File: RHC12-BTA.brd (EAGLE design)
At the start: 20 x 40 mm, 6 parts

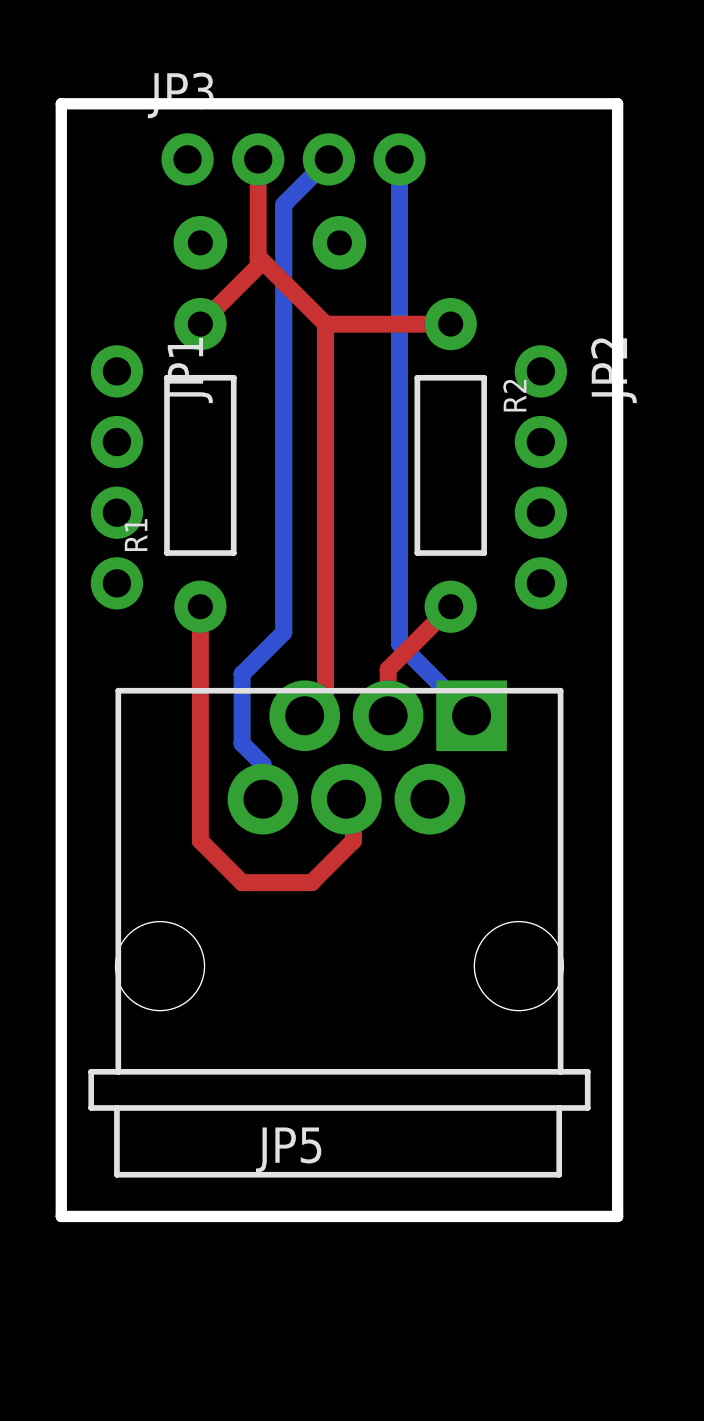
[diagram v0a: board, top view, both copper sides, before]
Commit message: Switched RHC12 to SMD except for the BTA part
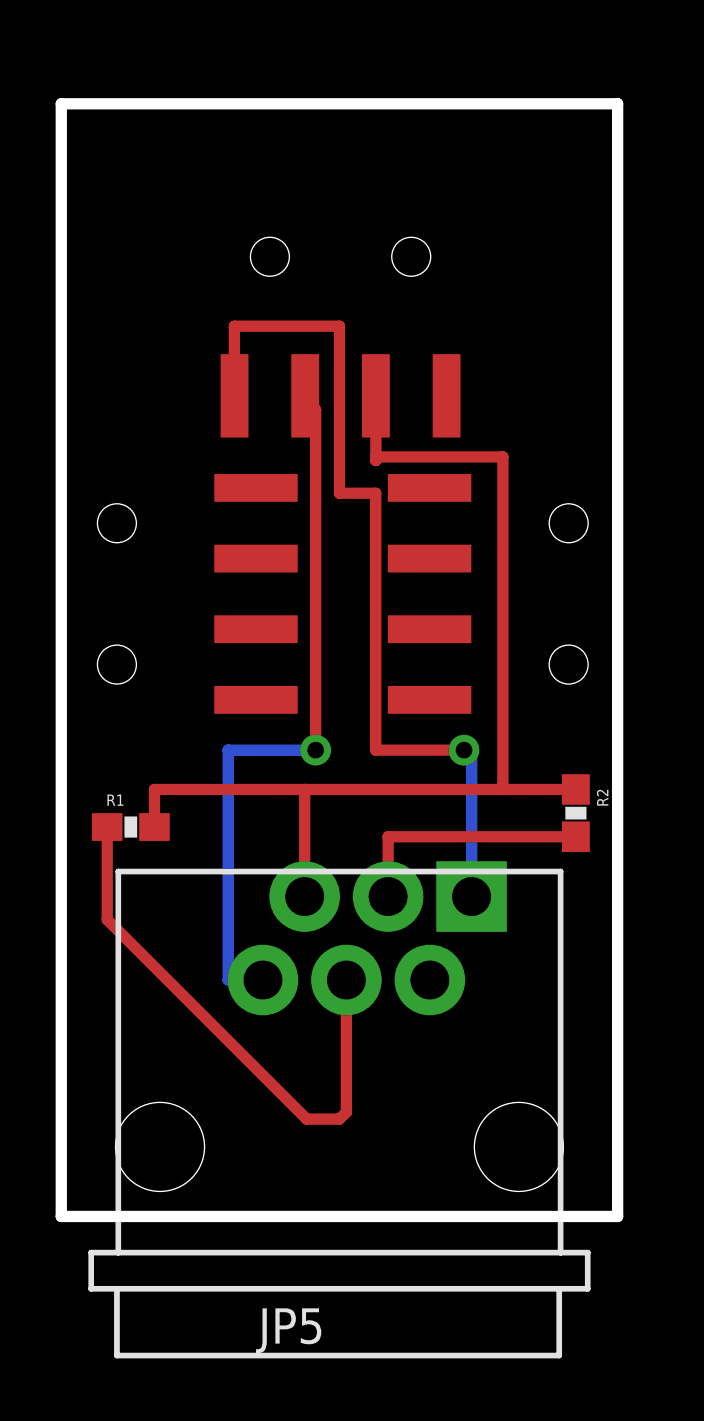
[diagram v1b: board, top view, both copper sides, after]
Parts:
- JP1, JP2, JP3: device SparkFun-Connectors:1X04_NO_SILK_ALL_ROUND -> SparkFun-Connectors:1X04-SMD
- R1, R2: device SparkFun-Passives:AXIAL-0.4 -> SparkFun-Passives:0603-RES
- moved R2 13.3 mm to (18.5, 14.5)
- moved R1 13.2 mm to (2.50, 14.0), turned to 0 degrees
- moved JP2 8.06 mm to (18.2, 22.4), turned to 90 degrees
- moved JP1 8.00 mm to (2.00, 22.4)
- moved JP3 6.52 mm to (10.0, 34.5), turned to 180 degrees
- moved JP5 6.50 mm to (10.0, 2.50)
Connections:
- net 5V: now also R1.2, R2.1; no longer R1.P$2, R2.P$1
- net N$1: now also R1.1; no longer R1.P$1
- net N$3: now also R2.2; no longer R2.P$2
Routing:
- net S2: track 21.1 -> 31.5 mm, vias 0 -> 1
- net 5V: track 29.1 -> 39.3 mm
- net N$3: track 4.85 -> 8.90 mm
- net N$1: track 16.8 -> 19.8 mm
- net S1: track 24.6 -> 27.6 mm, vias 0 -> 1
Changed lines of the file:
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@@
 <?xml version="1.0" encoding="utf-8"?>
 <!DOCTYPE eagle SYSTEM "eagle.dtd">
-<eagle version="7.5.0">
+<eagle version="7.2.0">
 <drawing>
 <settings>
@@
 </autorouter>
 <elements>
-<element name="JP5" library="SparkFun-Connectors" package="BTA" value="BTA" x="10" y="9"/>
-<element name="JP1" library="SparkFun-Connectors" package="1X04_NO_SILK_ALL_ROUND" value="" x="2" y="30.38" rot="R270"/>
-<element name="JP2" library="SparkFun-Connectors" package="1X04_NO_SILK_ALL_ROUND" value="" x="17.24" y="30.38" rot="R270"/>
-<element name="JP3" library="SparkFun-Connectors" package="1X04_NO_SILK_ALL_ROUND" value="" x="4.54" y="38"/>
-<element name="R1" library="SparkFun-Passives" package="AXIAL-0.4" value="" x="5" y="27" rot="R90"/>
-<element name="R2" library="SparkFun-Passives" package="AXIAL-0.4" value="" x="14" y="27" rot="R270"/>
+<element name="JP5" library="SparkFun-Connectors" package="BTA" value="BTA" x="10" y="2.5"/>
+<element name="JP1" library="SparkFun-Connectors" package="1X04-SMD" value="" x="2" y="22.38" rot="R270"/>
+<element name="JP2" library="SparkFun-Connectors" package="1X04-SMD" value="" x="18.24" y="22.38" rot="R90"/>
+<element name="JP3" library="SparkFun-Connectors" package="1X04-SMD" value="" x="10.04" y="34.5" rot="R180"/>
+<element name="R1" library="SparkFun-Passives" package="0603-RES" value="" x="2.5" y="14"/>
+<element name="R2" library="SparkFun-Passives" package="0603-RES" value="" x="18.5" y="14.5" rot="R270"/>
 </elements>
 <signals>
@@
 <contactref element="JP3" pad="2"/>
 <contactref element="JP5" pad="5"/>
-<contactref element="R1" pad="P$2"/>
-<contactref element="R2" pad="P$1"/>
-<wire x1="7.08" y1="38" x2="7.08" y2="34.5" width="0.6096" layer="1"/>
-<wire x1="7.08" y1="34.5" x2="7.08" y2="34.16" width="0.6096" layer="1"/>
-<wire x1="7.08" y1="34.16" x2="5" y2="32.08" width="0.6096" layer="1"/>
-<wire x1="14" y1="32.08" x2="9.5" y2="32.08" width="0.6096" layer="1"/>
-<wire x1="9.5" y1="32.08" x2="7.08" y2="34.5" width="0.6096" layer="1"/>
-<wire x1="9.5" y1="32.08" x2="9.5" y2="18.75" width="0.6096" layer="1"/>
-<wire x1="9.5" y1="18.75" x2="8.75" y2="18" width="0.6096" layer="1"/>
+<contactref element="R1" pad="2"/>
+<contactref element="R2" pad="1"/>
+<wire x1="18.5" y1="15.35" x2="15.875" y2="15.35" width="0.4064" layer="1"/>
+<wire x1="15.875" y1="15.35" x2="15.875" y2="27.305" width="0.4064" layer="1"/>
+<wire x1="15.875" y1="27.305" x2="11.303" y2="27.305" width="0.4064" layer="1"/>
+<wire x1="11.303" y1="27.305" x2="11.303" y2="27.178" width="0.4064" layer="1"/>
+<wire x1="11.303" y1="27.178" x2="11.31" y2="27.178" width="0.4064" layer="1"/>
+<wire x1="11.31" y1="27.178" x2="11.31" y2="29.5" width="0.4064" layer="1"/>
+<wire x1="15.875" y1="15.35" x2="8.75" y2="15.35" width="0.4064" layer="1"/>
+<wire x1="8.75" y1="15.35" x2="8.75" y2="11.5" width="0.4064" layer="1"/>
+<wire x1="3.35" y1="14" x2="3.35" y2="15.35" width="0.4064" layer="1"/>
+<wire x1="3.35" y1="15.35" x2="8.75" y2="15.35" width="0.4064" layer="1"/>
 </signal>
 <signal name="S1">
 <contactref element="JP3" pad="3"/>
 <contactref element="JP5" pad="6"/>
-<wire x1="7.25" y1="15" x2="7.25" y2="16.25" width="0.6096" layer="16"/>
-<wire x1="7.25" y1="16.25" x2="6.5" y2="17" width="0.6096" layer="16"/>
-<wire x1="6.5" y1="17" x2="6.5" y2="19.5" width="0.6096" layer="16"/>
-<wire x1="6.5" y1="19.5" x2="8" y2="21" width="0.6096" layer="16"/>
-<wire x1="8" y1="21" x2="8" y2="36.38" width="0.6096" layer="16"/>
-<wire x1="8" y1="36.38" x2="9.62" y2="38" width="0.6096" layer="16"/>
+<wire x1="6" y1="16.764" x2="9.144" y2="16.764" width="0.4064" layer="16"/>
+<via x="9.144" y="16.764" extent="1-16" drill="0.6" shape="square"/>
+<wire x1="9" y1="29" x2="9" y2="29.5" width="0.4064" layer="1"/>
+<wire x1="9" y1="29.5" x2="8.77" y2="29.5" width="0.4064" layer="1"/>
+<wire x1="9.144" y1="16.764" x2="9.144" y2="29" width="0.4064" layer="1"/>
+<wire x1="9.144" y1="29" x2="9" y2="29" width="0.4064" layer="1"/>
+<wire x1="7.25" y1="8.5" x2="6" y2="8.5" width="0.4064" layer="16"/>
+<wire x1="6" y1="8.5" x2="6" y2="16.764" width="0.4064" layer="16"/>
+<wire x1="6" y1="16.764" x2="5.996" y2="16.764" width="0.4064" layer="16"/>
+<wire x1="9.017" y1="28.238" x2="9.017" y2="29.5" width="0.4064" layer="1"/>
+<wire x1="9.017" y1="29.5" x2="9" y2="29.5" width="0.4064" layer="1"/>
+<wire x1="9" y1="29.5" x2="9" y2="30" width="0.4064" layer="1"/>
 </signal>
 <signal name="S2">
 <contactref element="JP3" pad="4"/>
 <contactref element="JP5" pad="1"/>
-<wire x1="12.16" y1="38" x2="12.16" y2="20.59" width="0.6096" layer="16"/>
-<wire x1="12.16" y1="20.59" x2="14.75" y2="18" width="0.6096" layer="16"/>
+<wire x1="14.75" y1="11.5" x2="14.75" y2="16.764" width="0.4064" layer="16"/>
+<wire x1="14.75" y1="16.764" x2="14.478" y2="16.764" width="0.4064" layer="16"/>
+<via x="14.478" y="16.764" extent="1-16" drill="0.6" shape="square"/>
+<wire x1="14.478" y1="16.764" x2="11.303" y2="16.764" width="0.4064" layer="1"/>
+<wire x1="11.303" y1="16.764" x2="11.303" y2="26" width="0.4064" layer="1"/>
+<wire x1="11.303" y1="26" x2="10" y2="26" width="0.4064" layer="1"/>
+<wire x1="10" y1="26" x2="10" y2="32.004" width="0.4064" layer="1"/>
+<wire x1="10" y1="32.004" x2="6.223" y2="32.004" width="0.4064" layer="1"/>
+<wire x1="6.223" y1="32.004" x2="6.223" y2="29.5" width="0.4064" layer="1"/>
+<wire x1="6.223" y1="29.5" x2="6.23" y2="29.5" width="0.4064" layer="1"/>
 </signal>
 <signal name="N$1">
 <contactref element="JP5" pad="4"/>
-<contactref element="R1" pad="P$1"/>
-<wire x1="5" y1="21.92" x2="5" y2="13.5" width="0.6096" layer="1"/>
-<wire x1="5" y1="13.5" x2="6.5" y2="12" width="0.6096" layer="1"/>
-<wire x1="6.5" y1="12" x2="9" y2="12" width="0.6096" layer="1"/>
-<wire x1="9" y1="12" x2="10.5" y2="13.5" width="0.6096" layer="1"/>
-<wire x1="10.5" y1="13.5" x2="10.5" y2="14.75" width="0.6096" layer="1"/>
-<wire x1="10.5" y1="14.75" x2="10.25" y2="15" width="0.6096" layer="1"/>
+<contactref element="R1" pad="1"/>
+<wire x1="10.25" y1="8.5" x2="10.25" y2="3.75" width="0.4064" layer="1"/>
+<wire x1="10.25" y1="3.75" x2="10" y2="3.5" width="0.4064" layer="1"/>
+<wire x1="10" y1="3.5" x2="8.819" y2="3.5" width="0.4064" layer="1"/>
+<wire x1="8.819" y1="3.5" x2="1.651" y2="10.668" width="0.4064" layer="1"/>
+<wire x1="1.651" y1="10.668" x2="1.651" y2="13.999" width="0.4064" layer="1"/>
+<wire x1="1.651" y1="13.999" x2="1.65" y2="14" width="0.4064" layer="1"/>
 </signal>
 <signal name="N$3">
-<contactref element="R2" pad="P$2"/>
+<contactref element="R2" pad="2"/>
 <contactref element="JP5" pad="3"/>
-<wire x1="11.75" y1="18" x2="11.75" y2="19.67" width="0.6096" layer="1"/>
-<wire x1="11.75" y1="19.67" x2="14" y2="21.92" width="0.6096" layer="1"/>
-</signal>
-<signal name="N$5">
-<via x="5" y="35" extent="1-16" drill="0.9" diameter="1.9304"/>
-</signal>
-<signal name="N$6">
-<via x="10" y="35" extent="1-16" drill="0.9" diameter="1.9304"/>
+<wire x1="11.75" y1="11.5" x2="11.75" y2="13.65" width="0.4064" layer="1"/>
+<wire x1="11.75" y1="13.65" x2="18.5" y2="13.65" width="0.4064" layer="1"/>
+</signal>
+<signal name="N$2">
+</signal>
+<signal name="N$4">
 </signal>
 </signals>
